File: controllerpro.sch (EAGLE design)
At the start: 10 parts

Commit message: Rename ports, add silkscreen port numbers
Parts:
- renumbered MULTI1 to PORT3, MULTI2 to PORT4, MULTI3 to PORT1, MULTI4 to PORT2

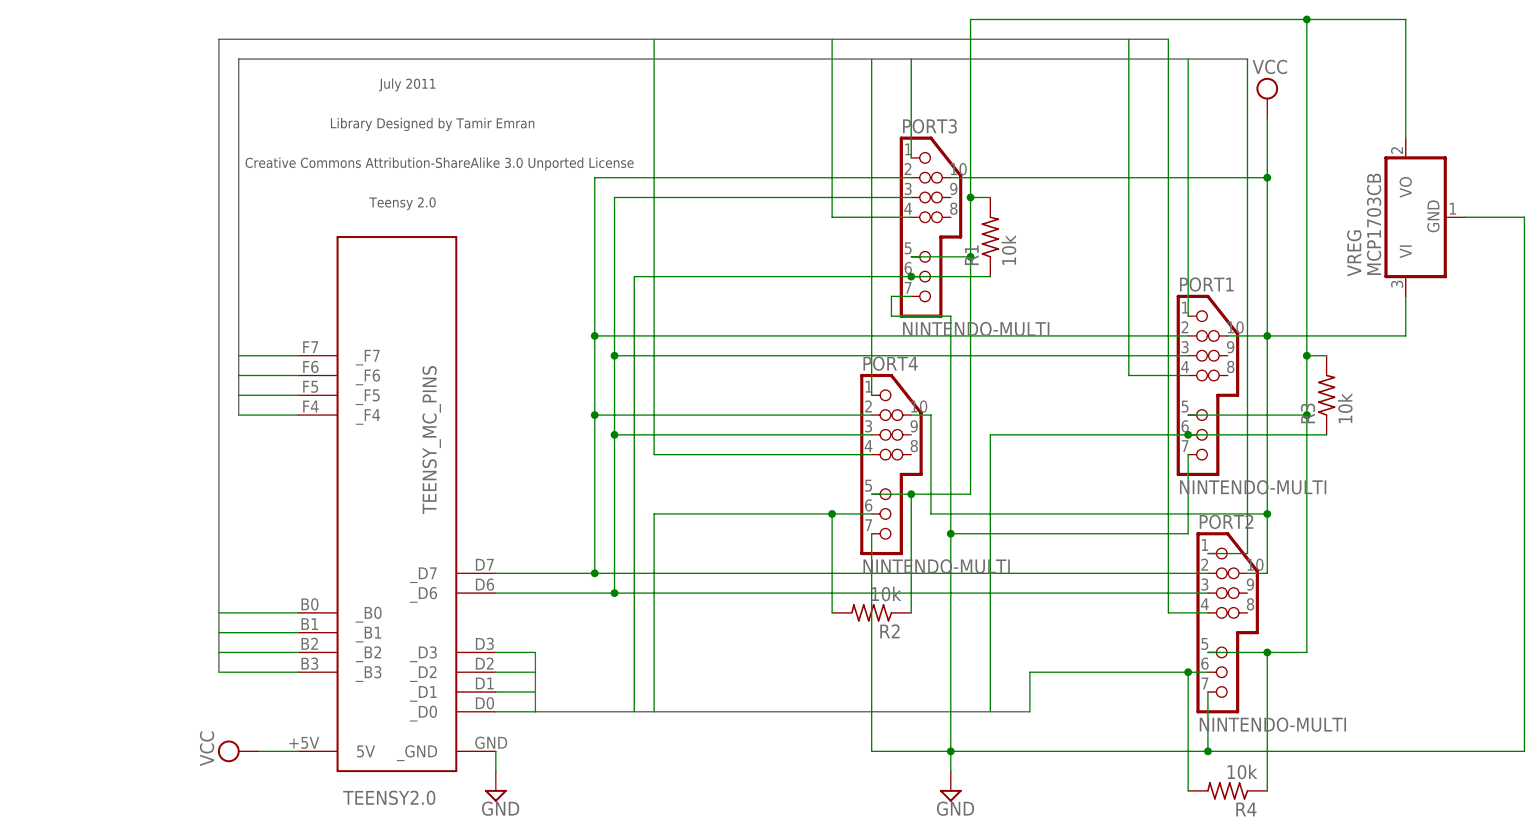
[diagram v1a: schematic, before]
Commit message: Update board for Bluetooth module
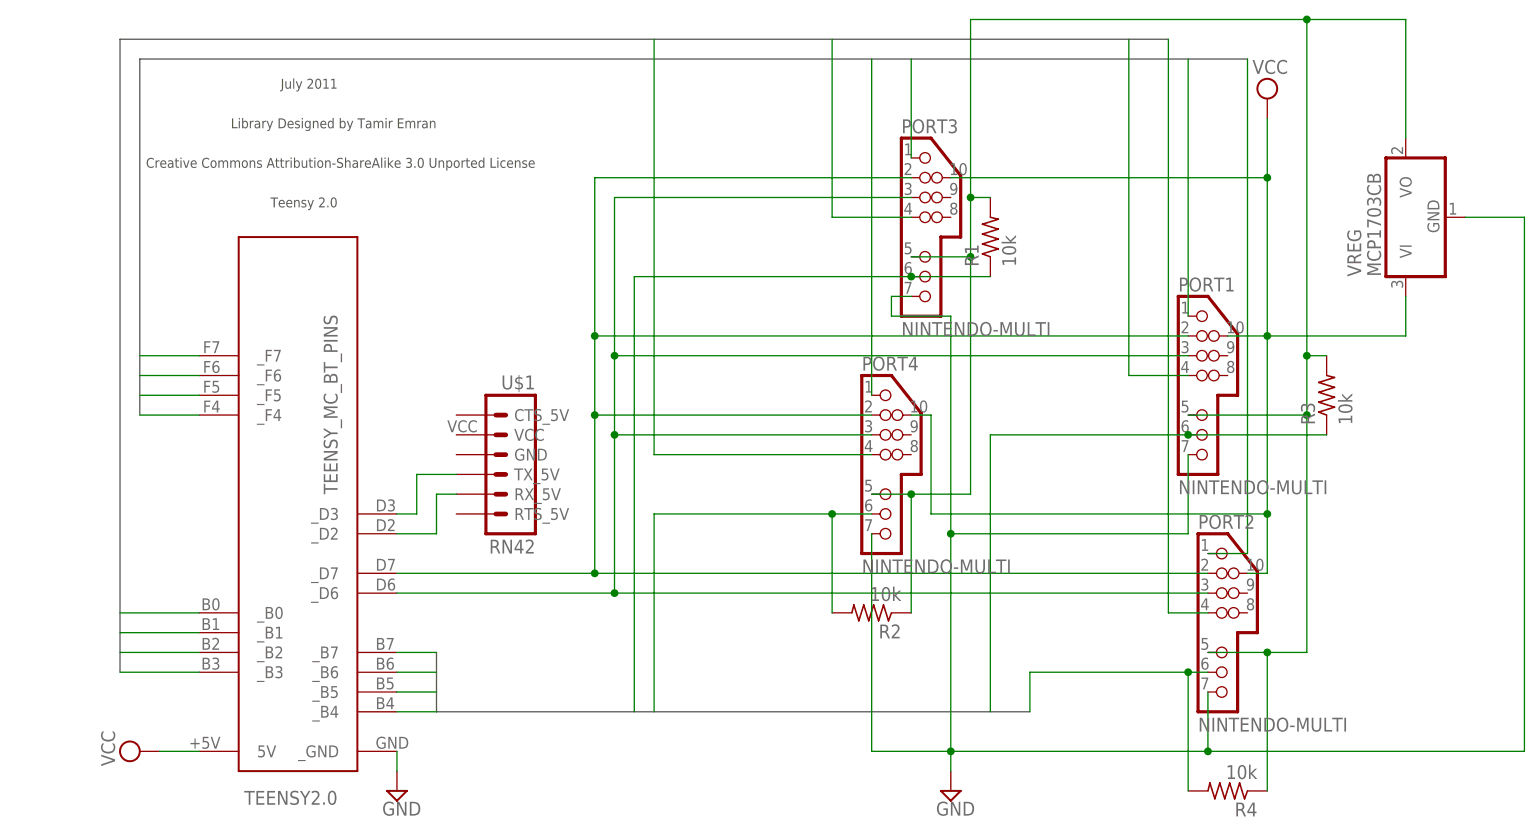
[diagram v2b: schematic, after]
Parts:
- added U$1: RN42, SparkFun-Boards:RN42
- TEENSY2.0: value TEENSY_MC_PINS -> TEENSY_MC_BT_PINS; device custom:TEENSY_MC_PINS -> custom:TEENSY_MC_BT_PINS
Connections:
- new net N$2: TEENSY2.0._D2, U$1.RX_5V
- new net N$5: TEENSY2.0._D3, U$1.TX_5V
- net 3VDATA0: now also TEENSY2.0._B6; no longer TEENSY2.0._D2
- net 3VDATA1: now also TEENSY2.0._B7; no longer TEENSY2.0._D3
- net 3VDATA2: now also TEENSY2.0._B4; no longer TEENSY2.0._D0
- net 3VDATA3: now also TEENSY2.0._B5; no longer TEENSY2.0._D1

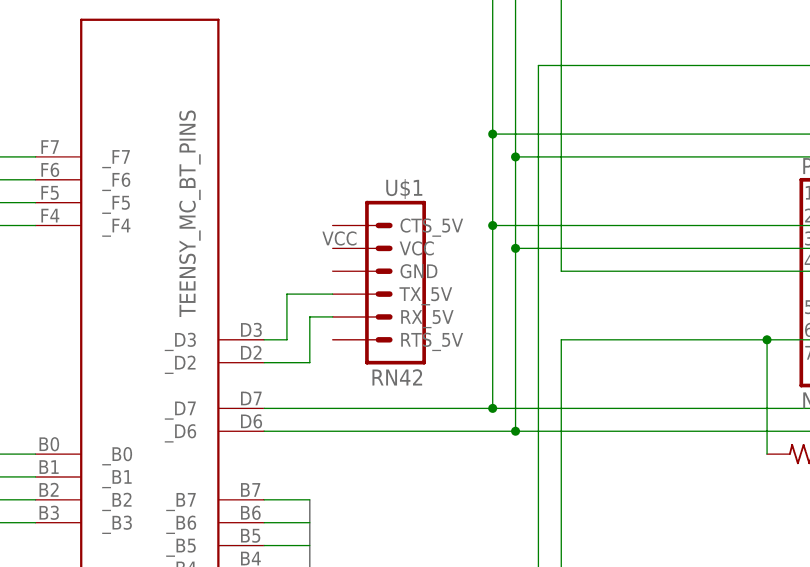
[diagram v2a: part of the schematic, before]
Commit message: Connect bluetooth power, etc:
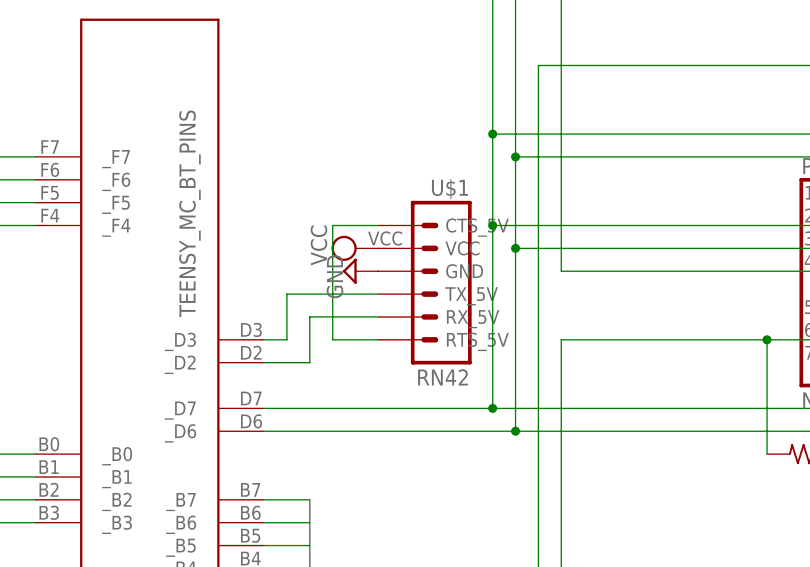
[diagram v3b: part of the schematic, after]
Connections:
- new net N$6: U$1.CTS_5V, U$1.RTS_5V
- net GND: now also U$1.GND
- net VCC: now also U$1.VCC
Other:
- moved on the sheet: U$1
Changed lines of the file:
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@@
 <grid distance="0.1" unitdist="inch" unit="inch" style="lines" multiple="1" display="no" altdistance="0.01" altunitdist="inch" altunit="inch"/>
 <layers>
-<layer number="1" name="Top" color="4" fill="1" visible="yes" active="no"/>
-<layer number="16" name="Bottom" color="1" fill="1" visible="yes" active="no"/>
-<layer number="17" name="Pads" color="2" fill="1" visible="yes" active="no"/>
-<layer number="18" name="Vias" color="2" fill="1" visible="yes" active="no"/>
-<layer number="19" name="Unrouted" color="6" fill="1" visible="yes" active="no"/>
-<layer number="20" name="Dimension" color="15" fill="1" visible="yes" active="no"/>
-<layer number="21" name="tPlace" color="7" fill="1" visible="yes" active="no"/>
-<layer number="22" name="bPlace" color="7" fill="1" visible="yes" active="no"/>
-<layer number="23" name="tOrigins" color="15" fill="1" visible="yes" active="no"/>
-<layer number="24" name="bOrigins" color="15" fill="1" visible="yes" active="no"/>
-<layer number="25" name="tNames" color="7" fill="1" visible="yes" active="no"/>
-<layer number="26" name="bNames" color="7" fill="1" visible="yes" active="no"/>
-<layer number="27" name="tValues" color="7" fill="1" visible="yes" active="no"/>
-<layer number="28" name="bValues" color="7" fill="1" visible="yes" active="no"/>
+<layer number="1" name="Top" color="4" fill="1" visible="no" active="no"/>
+<layer number="16" name="Bottom" color="1" fill="1" visible="no" active="no"/>
+<layer number="17" name="Pads" color="2" fill="1" visible="no" active="no"/>
+<layer number="18" name="Vias" color="2" fill="1" visible="no" active="no"/>
+<layer number="19" name="Unrouted" color="6" fill="1" visible="no" active="no"/>
+<layer number="20" name="Dimension" color="15" fill="1" visible="no" active="no"/>
+<layer number="21" name="tPlace" color="7" fill="1" visible="no" active="no"/>
+<layer number="22" name="bPlace" color="7" fill="1" visible="no" active="no"/>
+<layer number="23" name="tOrigins" color="15" fill="1" visible="no" active="no"/>
+<layer number="24" name="bOrigins" color="15" fill="1" visible="no" active="no"/>
+<layer number="25" name="tNames" color="7" fill="1" visible="no" active="no"/>
+<layer number="26" name="bNames" color="7" fill="1" visible="no" active="no"/>
+<layer number="27" name="tValues" color="7" fill="1" visible="no" active="no"/>
+<layer number="28" name="bValues" color="7" fill="1" visible="no" active="no"/>
 <layer number="29" name="tStop" color="7" fill="3" visible="no" active="no"/>
 <layer number="30" name="bStop" color="7" fill="6" visible="no" active="no"/>
@@
 <layer number="35" name="tGlue" color="7" fill="4" visible="no" active="no"/>
 <layer number="36" name="bGlue" color="7" fill="5" visible="no" active="no"/>
-<layer number="37" name="tTest" color="7" fill="1" visible="yes" active="no"/>
-<layer number="38" name="bTest" color="7" fill="1" visible="yes" active="no"/>
+<layer number="37" name="tTest" color="7" fill="1" visible="no" active="no"/>
+<layer number="38" name="bTest" color="7" fill="1" visible="no" active="no"/>
 <layer number="39" name="tKeepout" color="4" fill="11" visible="no" active="no"/>
 <layer number="40" name="bKeepout" color="1" fill="11" visible="no" active="no"/>
@@
 <layer number="44" name="Drills" color="7" fill="1" visible="no" active="no"/>
 <layer number="45" name="Holes" color="7" fill="1" visible="no" active="no"/>
-<layer number="46" name="Milling" color="3" fill="1" visible="yes" active="no"/>
-<layer number="47" name="Measures" color="7" fill="1" visible="yes" active="no"/>
-<layer number="48" name="Document" color="7" fill="1" visible="yes" active="no"/>
-<layer number="49" name="Reference" color="7" fill="1" visible="yes" active="no"/>
-<layer number="50" name="dxf" color="7" fill="1" visible="yes" active="no"/>
-<layer number="51" name="tDocu" color="7" fill="1" visible="yes" active="no"/>
-<layer number="52" name="bDocu" color="7" fill="1" visible="yes" active="no"/>
-<layer number="53" name="tGND_GNDA" color="7" fill="9" visible="yes" active="no"/>
-<layer number="54" name="bGND_GNDA" color="1" fill="9" visible="yes" active="no"/>
-<layer number="56" name="wert" color="7" fill="1" visible="yes" active="no"/>
+<layer number="46" name="Milling" color="3" fill="1" visible="no" active="no"/>
+<layer number="47" name="Measures" color="7" fill="1" visible="no" active="no"/>
+<layer number="48" name="Document" color="7" fill="1" visible="no" active="no"/>
+<layer number="49" name="Reference" color="7" fill="1" visible="no" active="no"/>
+<layer number="50" name="dxf" color="7" fill="1" visible="no" active="no"/>
+<layer number="51" name="tDocu" color="7" fill="1" visible="no" active="no"/>
+<layer number="52" name="bDocu" color="7" fill="1" visible="no" active="no"/>
+<layer number="53" name="tGND_GNDA" color="7" fill="9" visible="no" active="no"/>
+<layer number="54" name="bGND_GNDA" color="1" fill="9" visible="no" active="no"/>
+<layer number="56" name="wert" color="7" fill="1" visible="no" active="no"/>
 <layer number="91" name="Nets" color="2" fill="1" visible="yes" active="yes"/>
 <layer number="92" name="Busses" color="1" fill="1" visible="yes" active="yes"/>
@@
 <part name="R3" library="rcl" deviceset="R-US_" device="R0603" value="10k"/>
 <part name="U$1" library="SparkFun-Boards" deviceset="RN42" device=""/>
+<part name="SUPPLY4" library="supply2" deviceset="GND" device=""/>
+<part name="SUPPLY5" library="supply2" deviceset="VCC" device=""/>
 </parts>
 <sheets>
@@
 <instance part="R1" gate="G$1" x="129.54" y="86.36" rot="R90"/>
 <instance part="R3" gate="G$1" x="172.72" y="66.04" rot="R90"/>
-<instance part="U$1" gate="G$1" x="66.04" y="58.42" rot="MR0"/>
+<instance part="U$1" gate="G$1" x="71.12" y="58.42" rot="MR0"/>
+<instance part="SUPPLY4" gate="GND" x="63.5" y="58.42" rot="R270"/>
+<instance part="SUPPLY5" gate="G$1" x="63.5" y="60.96" rot="R90"/>
 </instances>
 <busses>
@@
 <pinref part="VREG" gate="G$1" pin="VI"/>
 <wire x1="182.88" y1="73.66" x2="182.88" y2="78.74" width="0.1524" layer="91"/>
+</segment>
+<segment>
+<pinref part="U$1" gate="G$1" pin="VCC"/>
+<pinref part="SUPPLY5" gate="G$1" pin="VCC"/>
 </segment>
 </net>
@@
 <pinref part="TEENSY2.0" gate="G$1" pin="_GND"/>
 <wire x1="53.34" y1="17.78" x2="53.34" y2="20.32" width="0.1524" layer="91"/>
+</segment>
+<segment>
+<pinref part="U$1" gate="G$1" pin="GND"/>
+<pinref part="SUPPLY4" gate="GND" pin="GND"/>
 </segment>
 </net>
@@
 <wire x1="58.42" y1="48.26" x2="58.42" y2="53.34" width="0.1524" layer="91"/>
 <pinref part="U$1" gate="G$1" pin="RX_5V"/>
-<wire x1="58.42" y1="53.34" x2="60.96" y2="53.34" width="0.1524" layer="91"/>
+<wire x1="58.42" y1="53.34" x2="66.04" y2="53.34" width="0.1524" layer="91"/>
 </segment>
 </net>
@@
 <wire x1="55.88" y1="50.8" x2="55.88" y2="55.88" width="0.1524" layer="91"/>
 <pinref part="U$1" gate="G$1" pin="TX_5V"/>
-<wire x1="55.88" y1="55.88" x2="60.96" y2="55.88" width="0.1524" layer="91"/>
-</segment>
-</net>
+<wire x1="55.88" y1="55.88" x2="66.04" y2="55.88" width="0.1524" layer="91"/>
+</segment>
+</net>
+<net name="N$6" class="0">
+<segment>
+<pinref part="U$1" gate="G$1" pin="CTS_5V"/>
+<wire x1="66.04" y1="63.5" x2="60.96" y2="63.5" width="0.1524" layer="91"/>
+<wire x1="60.96" y1="63.5" x2="60.96" y2="50.8" width="0.1524" layer="91"/>
+<pinref part="U$1" gate="G$1" pin="RTS_5V"/>
+<wire x1="60.96" y1="50.8" x2="66.04" y2="50.8" width="0.1524" layer="91"/>
+</segment>
+</net>
